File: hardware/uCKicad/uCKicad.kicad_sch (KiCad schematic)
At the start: 1 part

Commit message: Le microcontroleur sous KiCAD part 2
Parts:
- added C1: 4u7, symbol Device:C_Small
- added C10, C2, C3: 100n, symbol Device:C_Small
- added C5: 1u, symbol Device:C_Small
- added C7: 10n, symbol Device:C_Small
- added D1: ORANGE_TLMO110-GS8, symbol Device:LED_Small
- added L1: 39n, symbol Device:L_Small
- added R1: 1k, symbol Device:R_Small
- added R3: 100k, symbol Device:R_Small
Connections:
- net +3.3V: now also C1.1, C2.1, C3.1, L1.1
- net +3.3VA: now also C5.1, C7.1, L1.2
- net GND: now also C1.2, C10.2, C2.2, C3.2, C5.2, C7.2, R1.2, R3.2
- net NRST: now also C10.1
- net DAC_nCS: now reaches U?.10 (PA4)
- net SPI1_SCK: now reaches U?.11 (PA5)
- net SPI1_MOSI: now reaches U?.13 (PA7)
- net LED_STATUS: now reaches U?.18 (PA8)
- net LED_STATUS: now also D1.2 (A)
- net at U?.31 (PB9): now also R3.1
- net ADC_IN1: now reaches U?.7 (PA1)
- net DAC_nLDAC: now reaches U?.9 (PA3)
- new net: D1.1 (K), R1.1
- no-connect marks 0 -> 15

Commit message: Le reste du schema
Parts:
- added C11, C6: 1uF, symbol Device:C_Small
- added C8: 10u, symbol Device:C_Small
- added C9: 100n, symbol Device:C_Small
- added D2: ORANGE_TLMO110-GS8, symbol Device:LED_Small
- added J1: Conn_02x07_Odd_Even, symbol Connector_Generic:Conn_02x07_Odd_Even
- added J2: INPUT, symbol Connector_Generic:Conn_01x02
- added J3: OUTPUT, symbol Connector_Generic:Conn_01x02
- added J4: POWER, symbol Connector_Generic:Conn_01x02
- added R2: 1k, symbol Device:R_Small
- added U1: MCP1802x-xx02xOT, Package_TO_SOT_SMD:SOT-23-5, symbol Regulator_Linear:MCP1802x-xx02xOT
- added U2: MCP4801, symbol Analog_DAC:MCP4801
- gave numbers to parts that had none: 1
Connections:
- net +3.3V: now also C6.1, D2.2 (A), J1.3 (Pin_3), U1.5 (VOUT)
- net +3.3VA: now also C8.1, C9.1, U2.1 (Vdd), U2.6 (~{SHDN})
- net ADC_IN1: now also J2.1 (Pin_1)
- net DAC_nCS: now also U2.2 (~{CS})
- net DAC_nLDAC: now also U2.5 (~{LDAC})
- net GND: now also C8.2, C9.2, J1.11 (Pin_11), J1.5 (Pin_5), J1.7 (Pin_7), J2.2 (Pin_2), J3.2 (Pin_2), J4.2 (Pin_2), R2.2, U2.7 (Vss)
- net NRST: now also J1.12 (Pin_12)
- net SPI1_MOSI: now also U2.4 (SDI)
- net SPI1_SCK: now also U2.3 (SCK)
- net SWCLK: now also J1.6 (Pin_6)
- net SWDIO: now also J1.4 (Pin_4)
- net USART2_RX: now also J1.13 (Pin_13)
- net USART2_TX: now also J1.14 (Pin_14)
- new net: C11.2, C6.2, U1.2 (GND)
- new net: D2.1 (K), R2.1
- new net +5V: C11.1, J4.1 (Pin_1), U1.1 (VIN), U1.3 (~{SHDN})
- new net DAC_OUT: J3.1 (Pin_1), U2.8 (Vout)
- no-connect marks 15 -> 20
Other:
- moved on the sheet: C1, C10, C2, C3, C5, C7, D1, L1, R1, R3, U3

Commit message: on essaie de sauver le PC
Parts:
- C1, C10, C2, C3, C5, C7, C9: footprint (none) -> Capacitor_SMD:C_0805_2012Metric_Pad1.18x1.45mm_HandSolder
- C11, C6, C8: footprint (none) -> Capacitor_SMD:C_0805_2012Metric
- D1: footprint (none) -> LED_SMD:LED_0603_1608Metric_Pad1.05x0.95mm_HandSolder
- D2: value ORANGE_TLMO110-GS8 -> GREEN LED; footprint (none) -> LED_SMD:LED_0603_1608Metric_Pad1.05x0.95mm_HandSolder
- J1: footprint (none) -> Connector_PinHeader_1.27mm:PinHeader_2x07_P1.27mm_Vertical_SMD
- J2, J3, J4: footprint (none) -> Connector_JST:JST_XH_B2B-XH-A_1x02_P2.50mm_Vertical
- L1: footprint (none) -> Inductor_SMD:L_0805_2012Metric_Pad1.05x1.20mm_HandSolder
- R1, R2, R3: footprint (none) -> Resistor_SMD:R_0805_2012Metric_Pad1.20x1.40mm_HandSolder
- U1: value MCP1802x-xx02xOT -> BU33SD5WG-TR
- U2: footprint (none) -> Package_SO:SOIC-8_3.9x4.9mm_P1.27mm
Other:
- note added: "Alimentation"
- note added: "DAC MCP4801"
- note added: "IO Connector"
- note added: "SWD Connector"
- moved on the sheet: C1, C10, C2, C3, C5, C7, C8, C9, D1, J1, L1, R1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

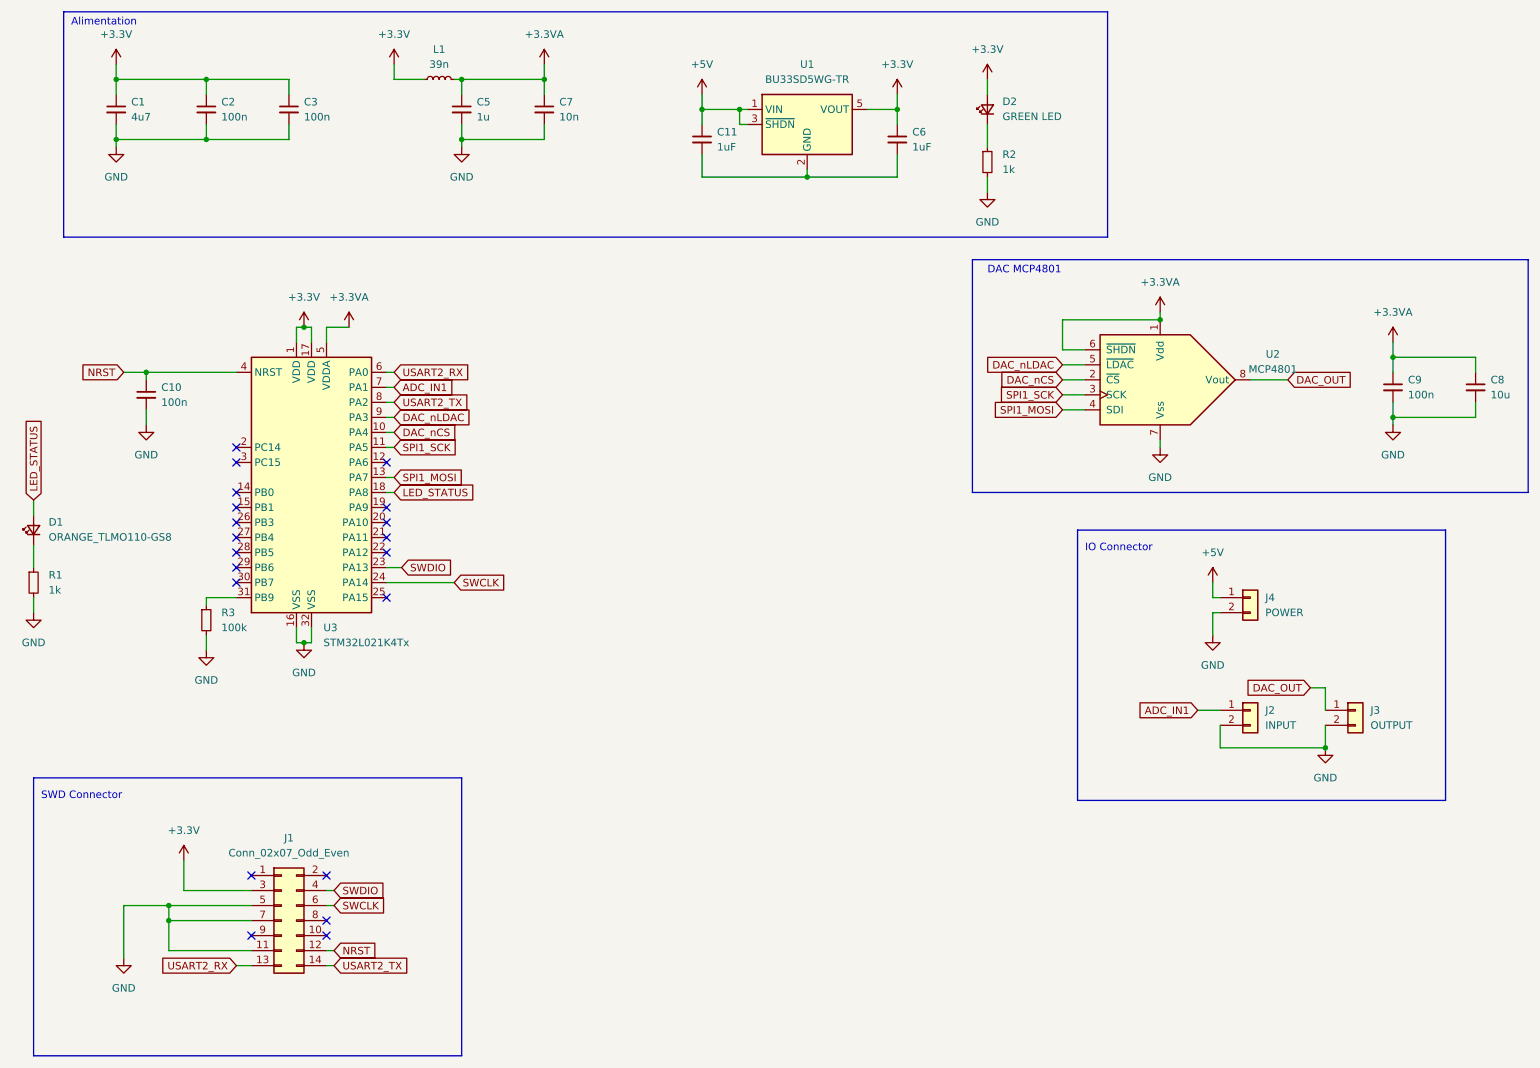
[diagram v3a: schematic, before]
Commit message: Placement des composants
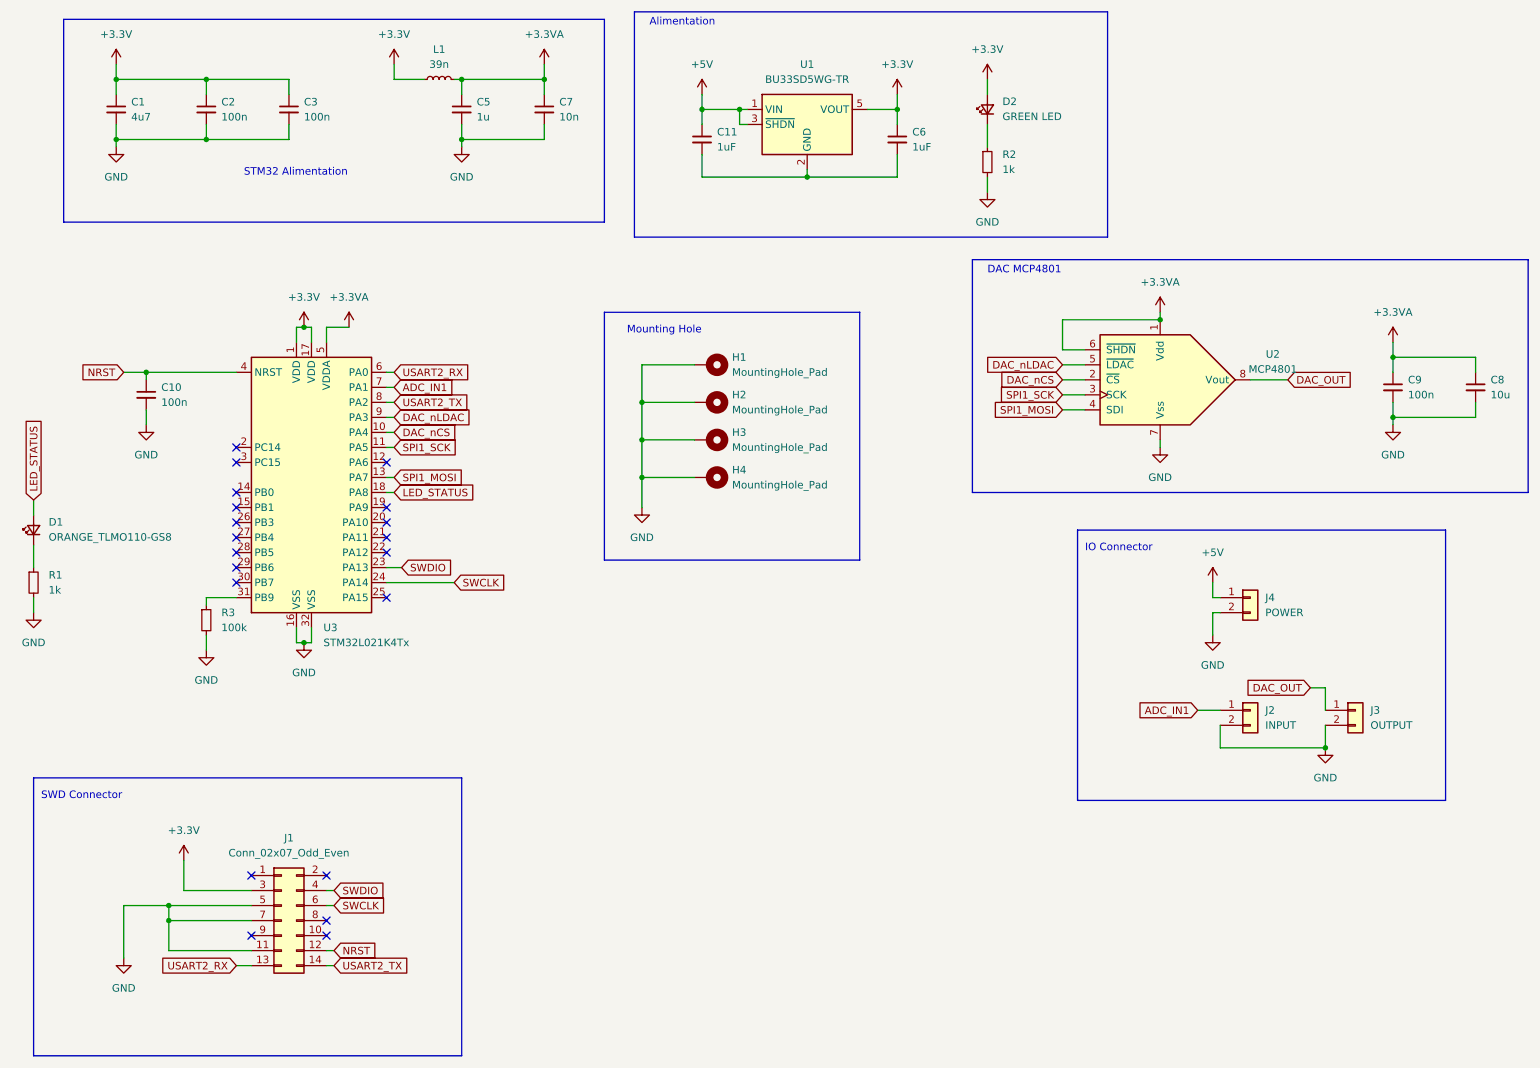
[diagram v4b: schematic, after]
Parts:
- added H1, H2, H3, H4: MountingHole_Pad, MountingHole:MountingHole_3.2mm_M3_Pad, symbol Mechanical:MountingHole_Pad
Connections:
- net GND: now also H1.1, H2.1, H3.1, H4.1
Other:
- note added: "Mounting Hole"
- note added: "STM32 Alimentation"

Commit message: Routage
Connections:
- net GND: now also C11.2, C6.2, U1.2 (GND)
- net BOOT0: now reaches R3.1, U3.31 (PB9)
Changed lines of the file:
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@@
   (junction (at 72.39 68.58) (diameter 0) (color 0 0 0 0)
+  )
+  (junction (at 140.97 43.18) (diameter 0) (color 0 0 0 0)
   )
   (junction (at 99.06 36.83) (diameter 0) (color 0 0 0 0)
@@
     (stroke (width 0) (type default) (color 0 0 0 0))
   )
-  (wire (pts (xy 157.48 43.18) (xy 139.7 43.18))
+  (wire (pts (xy 157.48 43.18) (xy 140.97 43.18))
     (stroke (width 0) (type default) (color 0 0 0 0))
   )
@@
   )
   (wire (pts (xy 187.96 26.67) (xy 187.96 29.21))
+    (stroke (width 0) (type default) (color 0 0 0 0))
+  )
+  (wire (pts (xy 140.97 43.18) (xy 139.7 43.18))
     (stroke (width 0) (type default) (color 0 0 0 0))
   )
@@
   (text "STM32 Alimentation" (at 62.23 43.18 0)
     (effects (font (size 1.27 1.27)) (justify left bottom))
+  )
+  (label "BOOT0" (at 55.88 114.3 180)
+    (effects (font (size 1.27 1.27)) (justify right bottom))
   )
   (global_label "DAC_nLDAC" (shape input) (at 200.66 74.93 180) (fields_autoplaced)
@@
     )
     (property "Datasheet" "" (id 3) (at 40.64 24.13 0)
+      (effects (font (size 1.27 1.27)) hide)
+    )
+    (pin "1")
+  )
+  (symbol (lib_id "power:GND") (at 140.97 43.18 0) (unit 1)
+    (in_bom yes) (on_board yes) (fields_autoplaced)
+    (property "Reference" "#PWR0102" (id 0) (at 140.97 49.53 0)
+      (effects (font (size 1.27 1.27)) hide)
+    )
+    (property "Value" "GND" (id 1) (at 140.97 48.26 0))
+    (property "Footprint" "" (id 2) (at 140.97 43.18 0)
+      (effects (font (size 1.27 1.27)) hide)
+    )
+    (property "Datasheet" "" (id 3) (at 140.97 43.18 0)
       (effects (font (size 1.27 1.27)) hide)
     )
@@
       (reference "#PWR0101") (unit 1) (value "GND") (footprint "")
     )
+    (path "/24f46001-6c89-483a-9e61-4ec498efa62a"
+      (reference "#PWR0102") (unit 1) (value "GND") (footprint "")
+    )
     (path "/80af4768-0d70-4a6d-a712-e1b9e5e141a6"
